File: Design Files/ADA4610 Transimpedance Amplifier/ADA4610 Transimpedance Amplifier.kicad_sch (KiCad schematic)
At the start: 33 parts, among them J1 Conn_01x03_Male, J2 Conn_Coaxial, U1 ADA4610-1xR, U2 ADA4610-1xR

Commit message: Gave a quick schematic review
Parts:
- TP1, TP4: value TestPoint -> TP_GND
- TP2: value TestPoint -> TP_V+
- TP3: value TestPoint -> TP_V-
- TP5: value TestPoint -> TP_TIA_OUT
- TP6: value TestPoint -> TP_OUTPUT
- TP7: value TestPoint -> TP_OUTPUT_50OHM
- U1, U2: footprint Package_TO_SOT_SMD:SOT-23-5_HandSoldering -> Package_TO_SOT_SMD:SOT-23-5; symbol ADA4610_Transimpedance_Amplifier_REV1:ADA4610-1xR -> Amplifier_Operational:ADA4610-1xRJ
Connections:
- net VCC: now also U1.5 (V+), U2.5 (V+); no longer U1.7 (V+), U2.7 (V+)
- net VEE: now also U1.2 (V-), U2.2 (V-); no longer U1.4 (V-), U2.4 (V-)
- net at C4.1, D1.1 (K), R6.1: now also U1.4 (-); no longer U1.2 (-)
- net at C4.2, R6.2, TP5.1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: now also U1.1; no longer U1.6
- net at R8.1, R9.2, TP6.1: now also U2.1; no longer U2.6
- net at R7.2, R8.2: now also U2.4 (-); no longer U2.2 (-)
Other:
- note added: "Av = 1+ R8/R7 = 50.9 V/V"
- note added: "Photoconductive Mode Negative Reverse Bias"
- note added: "Photovoltaic Mode Zero Bias (When Op-Amp Vref = GND)"
- note added: "Vout = Id*R6"
- note added: "fmax = sqrt(ft/(2*pi*Rf*Cf)) = 2.12MHz ft = Unity Gain = 9.3Mhz"
- note removed: "Av = 50 V/V"
- note removed: "Negative Reverse Bias"
- note removed: "Vout = Id*100k"
- note removed: "Zero Bias (When Op-Amp Vref = GND)"
- note removed: "fmax = sqrt(ft/(2*pi*Rf*Cf)) ft = Unity Gain = 9.3Mhz"
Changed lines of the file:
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@@
     (effects (font (size 1.27 1.27)) (justify left bottom))
   )
-  (text "fmax = sqrt(ft/(2*pi*Rf*Cf))\nft = Unity Gain = 9.3Mhz\n\n\n"
+  (text "fmax = sqrt(ft/(2*pi*Rf*Cf)) = 2.12MHz\nft = Unity Gain = 9.3Mhz\n\n\n"
     (at 110.49 160.02 0)
     (effects (font (size 1.27 1.27)) (justify left bottom))
@@
     (effects (font (size 1.27 1.27)) (justify left bottom))
   )
-  (text "Vout = Id*100k" (at 110.49 148.59 0)
-    (effects (font (size 1.27 1.27)) (justify left bottom))
-  )
-  (text "Zero Bias\n(When Op-Amp Vref = GND)" (at 52.07 163.83 90)
-    (effects (font (size 1.27 1.27)) (justify left bottom))
-  )
-  (text "Negative Reverse Bias" (at 41.91 163.83 90)
+  (text "Vout = Id*R6" (at 110.49 148.59 0)
+    (effects (font (size 1.27 1.27)) (justify left bottom))
+  )
+  (text "Photovoltaic Mode\nZero Bias\n(When Op-Amp Vref = GND)"
+    (at 52.07 163.83 90)
+    (effects (font (size 1.27 1.27)) (justify left bottom))
+  )
+  (text "Photoconductive Mode\nNegative Reverse Bias" (at 41.91 163.83 90)
     (effects (font (size 1.27 1.27)) (justify left bottom))
   )
@@
     (effects (font (size 1.27 1.27)) (justify left bottom))
   )
-  (text "Av = 50 V/V" (at 176.53 130.81 0)
+  (text "Av = 1+ R8/R7 = 50.9 V/V" (at 176.53 130.81 0)
     (effects (font (size 1.27 1.27)) (justify left bottom))
   )
@@
       (effects (font (size 1.27 1.27)) (justify left))
     )
-    (property "Value" "TestPoint" (id 1) (at 247.65 83.0579 0)
+    (property "Value" "TP_OUTPUT_50OHM" (id 1) (at 247.65 83.0579 0)
       (effects (font (size 1.27 1.27)) (justify left))
     )
@@
     )
   )
-  (symbol (lib_id "ADA4610_Transimpedance_Amplifier_REV1:ADA4610-1xR") (at 184.15 95.25 0) (unit 1)
+  (symbol (lib_id "Amplifier_Operational:ADA4610-1xRJ") (at 184.15 95.25 0) (unit 1)
     (in_bom yes) (on_board yes) (fields_autoplaced)
     (property "Reference" "U2" (id 0) (at 196.85 90.551 0))
     (property "Value" "ADA4610-1xR" (id 1) (at 196.85 93.091 0))
-    (property "Footprint" "Package_TO_SOT_SMD:SOT-23-5_HandSoldering" (id 2) (at 181.61 100.33 0)
+    (property "Footprint" "Package_TO_SOT_SMD:SOT-23-5" (id 2) (at 181.61 100.33 0)
       (effects (font (size 1.27 1.27)) (justify left) hide)
     )
-    (property "Datasheet" "https://www.analog.com/media/en/technical-documentation/data-sheets/ADA4610-1_4610-2_4610-4.pdf" (id 3) (at 187.96 91.44 0)
-      (effects (font (size 1.27 1.27)) hide)
-    )
-    (pin "1")
-    (pin "2")
+    (property "Datasheet" "https://www.analog.com/media/en/technical-documentation/data-sheets/ADA4610-1_4610-2_4610-4.pdf" (id 3) (at 184.15 90.17 0)
+      (effects (font (size 1.27 1.27)) hide)
+    )
+    (pin "2")
+    (pin "5")
+    (pin "1")
     (pin "3")
     (pin "4")
-    (pin "5")
-    (pin "6")
-    (pin "7")
-    (pin "8")
   )
   (symbol (lib_id "Device:R_US") (at 40.64 120.65 0) (unit 1)
@@
       (effects (font (size 1.27 1.27)) (justify left))
     )
-    (property "Value" "TestPoint" (id 1) (at 39.37 23.3679 0)
+    (property "Value" "TP_V+" (id 1) (at 39.37 23.3679 0)
       (effects (font (size 1.27 1.27)) (justify left))
     )
@@
       (effects (font (size 1.27 1.27)) (justify right))
     )
-    (property "Value" "TestPoint" (id 1) (at 39.37 40.1319 0)
+    (property "Value" "TP_V-" (id 1) (at 39.37 40.1319 0)
       (effects (font (size 1.27 1.27)) (justify right))
     )
@@
       (effects (font (size 1.27 1.27)) (justify left))
     )
-    (property "Value" "TestPoint" (id 1) (at 209.55 83.0579 0)
+    (property "Value" "TP_OUTPUT" (id 1) (at 209.55 83.0579 0)
       (effects (font (size 1.27 1.27)) (justify left))
     )
@@
     )
   )
-  (symbol (lib_id "ADA4610_Transimpedance_Amplifier_REV1:ADA4610-1xR") (at 115.57 92.71 0) (unit 1)
+  (symbol (lib_id "Amplifier_Operational:ADA4610-1xRJ") (at 115.57 92.71 0) (unit 1)
     (in_bom yes) (on_board yes) (fields_autoplaced)
     (property "Reference" "U1" (id 0) (at 128.27 88.011 0))
     (property "Value" "ADA4610-1xR" (id 1) (at 128.27 90.551 0))
-    (property "Footprint" "Package_TO_SOT_SMD:SOT-23-5_HandSoldering" (id 2) (at 113.03 97.79 0)
+    (property "Footprint" "Package_TO_SOT_SMD:SOT-23-5" (id 2) (at 113.03 97.79 0)
       (effects (font (size 1.27 1.27)) (justify left) hide)
     )
-    (property "Datasheet" "https://www.analog.com/media/en/technical-documentation/data-sheets/ADA4610-1_4610-2_4610-4.pdf" (id 3) (at 119.38 88.9 0)
-      (effects (font (size 1.27 1.27)) hide)
-    )
-    (pin "1")
-    (pin "2")
+    (property "Datasheet" "https://www.analog.com/media/en/technical-documentation/data-sheets/ADA4610-1_4610-2_4610-4.pdf" (id 3) (at 115.57 87.63 0)
+      (effects (font (size 1.27 1.27)) hide)
+    )
+    (pin "2")
+    (pin "5")
+    (pin "1")
     (pin "3")
     (pin "4")
-    (pin "5")
-    (pin "6")
-    (pin "7")
-    (pin "8")
   )
   (symbol (lib_id "Device:R_US") (at 96.52 116.84 0) (unit 1)
@@
       (effects (font (size 1.27 1.27)) (justify left))
     )
-    (property "Value" "TestPoint" (id 1) (at 212.09 30.9879 0)
+    (property "Value" "TP_GND" (id 1) (at 212.09 30.9879 0)
       (effects (font (size 1.27 1.27)) (justify left))
     )
@@
       (effects (font (size 1.27 1.27)) (justify left))
     )
-    (property "Value" "TestPoint" (id 1) (at 227.33 30.9879 0)
+    (property "Value" "TP_GND" (id 1) (at 227.33 30.9879 0)
       (effects (font (size 1.27 1.27)) (justify left))
     )
@@
       (effects (font (size 1.27 1.27)) (justify left))
     )
-    (property "Value" "TestPoint" (id 1) (at 146.05 90.6779 0)
+    (property "Value" "TP_TIA_OUT" (id 1) (at 146.05 90.6779 0)
       (effects (font (size 1.27 1.27)) (justify left))
     )
@@
     )
     (path "/e1dc39f6-a64b-409c-8102-e31f54d2c490"
-      (reference "TP1") (unit 1) (value "TestPoint") (footprint "TestPoint:TestPoint_Keystone_5010-5014_Multipurpose")
+      (reference "TP1") (unit 1) (value "TP_GND") (footprint "TestPoint:TestPoint_Keystone_5010-5014_Multipurpose")
     )
     (path "/77d853be-d651-447f-a5fb-1f44a94285db"
-      (reference "TP2") (unit 1) (value "TestPoint") (footprint "TestPoint:TestPoint_Keystone_5010-5014_Multipurpose")
+      (reference "TP2") (unit 1) (value "TP_V+") (footprint "TestPoint:TestPoint_Keystone_5010-5014_Multipurpose")
     )
     (path "/94e8d591-6962-47bb-94fb-370f42ef4ca2"
-      (reference "TP3") (unit 1) (value "TestPoint") (footprint "TestPoint:TestPoint_Keystone_5010-5014_Multipurpose")
+      (reference "TP3") (unit 1) (value "TP_V-") (footprint "TestPoint:TestPoint_Keystone_5010-5014_Multipurpose")
     )
     (path "/e5ae9f37-327f-4940-9b1e-8619a7f0246f"
-      (reference "TP4") (unit 1) (value "TestPoint") (footprint "TestPoint:TestPoint_Keystone_5010-5014_Multipurpose")
+      (reference "TP4") (unit 1) (value "TP_GND") (footprint "TestPoint:TestPoint_Keystone_5010-5014_Multipurpose")
     )
     (path "/e620e2d6-b792-4e72-96c4-53350b73578f"
-      (reference "TP5") (unit 1) (value "TestPoint") (footprint "TestPoint:TestPoint_Keystone_5010-5014_Multipurpose")
+      (reference "TP5") (unit 1) (value "TP_TIA_OUT") (footprint "TestPoint:TestPoint_Keystone_5010-5014_Multipurpose")
     )
     (path "/c101dbe3-d377-45c1-8c3f-5c0a91d1494e"
-      (reference "TP6") (unit 1) (value "TestPoint") (footprint "TestPoint:TestPoint_Keystone_5010-5014_Multipurpose")
+      (reference "TP6") (unit 1) (value "TP_OUTPUT") (footprint "TestPoint:TestPoint_Keystone_5010-5014_Multipurpose")
     )
     (path "/0d3b6448-884c-4656-9607-90a1b575d3f4"
-      (reference "TP7") (unit 1) (value "TestPoint") (footprint "TestPoint:TestPoint_Keystone_5010-5014_Multipurpose")
+      (reference "TP7") (unit 1) (value "TP_OUTPUT_50OHM") (footprint "TestPoint:TestPoint_Keystone_5010-5014_Multipurpose")
     )
     (path "/d40ba23e-8518-42c3-b6f8-270decb2e700"
-      (reference "U1") (unit 1) (value "ADA4610-1xR") (footprint "Package_TO_SOT_SMD:SOT-23-5_HandSoldering")
+      (reference "U1") (unit 1) (value "ADA4610-1xR") (footprint "Package_TO_SOT_SMD:SOT-23-5")
     )
     (path "/6465df4d-151b-4266-bd35-340202650477"
-      (reference "U2") (unit 1) (value "ADA4610-1xR") (footprint "Package_TO_SOT_SMD:SOT-23-5_HandSoldering")
-    )
-  )
+      (reference "U2") (unit 1) (value "ADA4610-1xR") (footprint "Package_TO_SOT_SMD:SOT-23-5")
+    )
+  )

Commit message: Initial Placement Done.
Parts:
- D1: footprint Package_TO_SOT_THT:TO-18-2_Lens -> ADA4610-transimpedance-amplifier:TO-18-2_Lens_Centered
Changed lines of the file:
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@@
       (effects (font (size 1.27 1.27)) (justify left))
     )
-    (property "Footprint" "Package_TO_SOT_THT:TO-18-2_Lens" (id 2) (at 50.8 105.41 0)
+    (property "Footprint" "ADA4610-transimpedance-amplifier:TO-18-2_Lens_Centered" (id 2) (at 50.8 105.41 0)
       (effects (font (size 1.27 1.27)) hide)
     )
@@
     )
     (path "/77fe5954-2f88-4ed4-92bc-bc3cc4ac221b"
-      (reference "D1") (unit 1) (value "ODD-1W") (footprint "Package_TO_SOT_THT:TO-18-2_Lens")
+      (reference "D1") (unit 1) (value "ODD-1W") (footprint "ADA4610-transimpedance-amplifier:TO-18-2_Lens_Centered")
     )
     (path "/0e9ad7f4-e2e4-4f66-a3cd-b654f2049983"

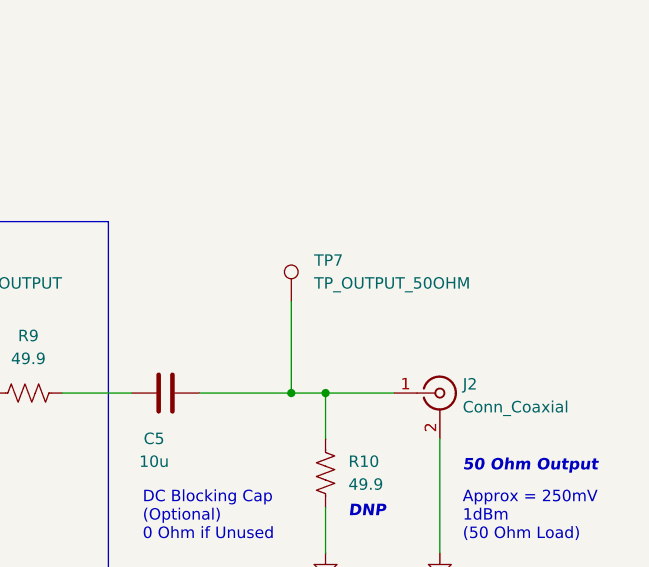
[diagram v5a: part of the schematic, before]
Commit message: Placement and text completed.
Ready for traces.
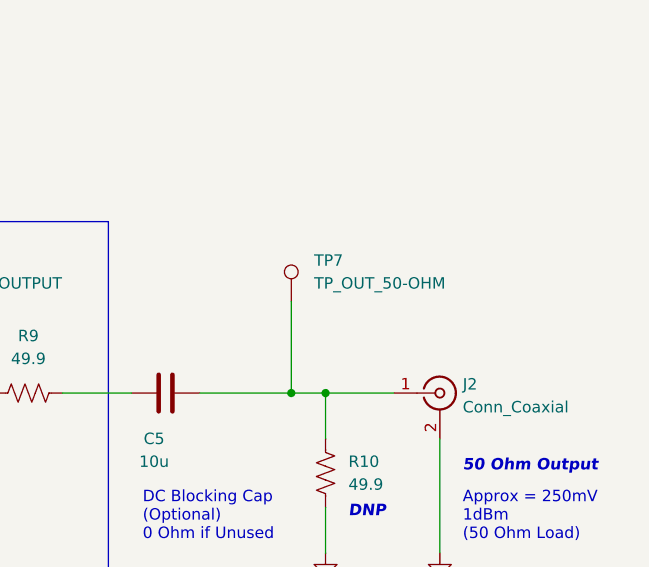
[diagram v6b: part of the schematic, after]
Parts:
- TP7: value TP_OUTPUT_50OHM -> TP_OUT_50-OHM
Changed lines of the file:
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@@
       (effects (font (size 1.27 1.27)) (justify left))
     )
-    (property "Value" "TP_OUTPUT_50OHM" (id 1) (at 247.65 83.0579 0)
+    (property "Value" "TP_OUT_50-OHM" (id 1) (at 247.65 83.0579 0)
       (effects (font (size 1.27 1.27)) (justify left))
     )
@@
     )
     (path "/0d3b6448-884c-4656-9607-90a1b575d3f4"
-      (reference "TP7") (unit 1) (value "TP_OUTPUT_50OHM") (footprint "TestPoint:TestPoint_Keystone_5010-5014_Multipurpose")
+      (reference "TP7") (unit 1) (value "TP_OUT_50-OHM") (footprint "TestPoint:TestPoint_Keystone_5010-5014_Multipurpose")
     )
     (path "/d40ba23e-8518-42c3-b6f8-270decb2e700"

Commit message: Board completed and no errors.
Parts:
- removed TP7: TP_OUT_50-OHM, TestPoint:TestPoint_Keystone_5010-5014_Multipurpose, symbol Connector:TestPoint
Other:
- note added: "Note: Frequencies are low enough to not actually cause much concern here"
- note added: "Rough 50 Ohm Spec per Twitter @tedyapo - Osh Park 2 Layer 62 mil board - 22 mil trace above ground - 6 mil side pour GND clearance -15.748mil (0.4mm) vias -- Spaced 50 mils from either side of trace -- 100 mil spacings"
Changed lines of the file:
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@@
   (junction (at 162.56 121.92) (diameter 0) (color 0 0 0 0)
   )
-  (junction (at 245.11 95.25) (diameter 0) (color 0 0 0 0)
-  )
   (junction (at 83.82 90.17) (diameter 0) (color 0 0 0 0)
   )
@@
     (stroke (width 0) (type default) (color 0 0 0 0))
   )
-  (wire (pts (xy 245.11 85.09) (xy 245.11 95.25))
-    (stroke (width 0) (type default) (color 0 0 0 0))
-  )
   (wire (pts (xy 73.66 31.75) (xy 73.66 36.83))
     (stroke (width 0) (type default) (color 0 0 0 0))
@@
     (stroke (width 0) (type default) (color 0 0 0 0))
   )
-  (wire (pts (xy 234.95 95.25) (xy 245.11 95.25))
-    (stroke (width 0) (type default) (color 0 0 0 0))
-  )
   (wire (pts (xy 69.85 123.19) (xy 83.82 123.19))
     (stroke (width 0) (type default) (color 0 0 0 0))
@@
     (stroke (width 0) (type default) (color 0 0 0 0))
   )
-  (wire (pts (xy 245.11 95.25) (xy 248.92 95.25))
+  (wire (pts (xy 234.95 95.25) (xy 248.92 95.25))
     (stroke (width 0) (type default) (color 0 0 0 0))
   )
@@
     (effects (font (size 1.27 1.27) (thickness 0.254) bold italic) (justify left bottom))
   )
+  (text "Note: Frequencies are low enough to not actually cause much concern here"
+    (at 208.28 165.1 0)
+    (effects (font (size 1.27 1.27)) (justify left bottom))
+  )
   (text "Vcc = +5V to +15V\nVee = -5V to -15V\n" (at 257.81 132.08 0)
     (effects (font (size 1.27 1.27)) (justify left bottom))
@@
     (effects (font (size 2.5 2.5) (thickness 0.5) bold) (justify left bottom))
   )
+  (text "Rough 50 Ohm Spec per Twitter @tedyapo\n- Osh Park 2 Layer 62 mil board\n- 22 mil trace above ground\n- 6 mil side pour GND clearance\n-15.748mil (0.4mm) vias\n-- Spaced 50 mils from either side of trace\n-- 100 mil spacings\n\n"
+    (at 233.68 149.86 0)
+    (effects (font (size 1.27 1.27)) (justify left bottom))
+  )
   (text "DNP" (at 53.34 125.73 0)
     (effects (font (size 1.27 1.27) (thickness 0.254) bold italic) (justify left bottom))
@@
     (pin "1")
     (pin "2")
-  )
-  (symbol (lib_id "Connector:TestPoint") (at 245.11 85.09 0) (unit 1)
-    (in_bom yes) (on_board yes) (fields_autoplaced)
-    (property "Reference" "TP7" (id 0) (at 247.65 80.5179 0)
-      (effects (font (size 1.27 1.27)) (justify left))
-    )
-    (property "Value" "TP_OUT_50-OHM" (id 1) (at 247.65 83.0579 0)
-      (effects (font (size 1.27 1.27)) (justify left))
-    )
-    (property "Footprint" "TestPoint:TestPoint_Keystone_5010-5014_Multipurpose" (id 2) (at 250.19 85.09 0)
-      (effects (font (size 1.27 1.27)) hide)
-    )
-    (property "Datasheet" "~" (id 3) (at 250.19 85.09 0)
-      (effects (font (size 1.27 1.27)) hide)
-    )
-    (pin "1")
   )
   (symbol (lib_id "Mechanical:MountingHole") (at 252.73 24.13 0) (unit 1)
@@
       (reference "TP6") (unit 1) (value "TP_OUTPUT") (footprint "TestPoint:TestPoint_Keystone_5010-5014_Multipurpose")
     )
-    (path "/0d3b6448-884c-4656-9607-90a1b575d3f4"
-      (reference "TP7") (unit 1) (value "TP_OUT_50-OHM") (footprint "TestPoint:TestPoint_Keystone_5010-5014_Multipurpose")
-    )
     (path "/d40ba23e-8518-42c3-b6f8-270decb2e700"
